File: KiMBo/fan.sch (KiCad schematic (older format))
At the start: 36 parts, among them Q4 2N7002, Q5 DMP3098L-7, Q6 2N7002, Q7 DMP3098L-7, Q8 2N7002, Q9 DMP3098L-7

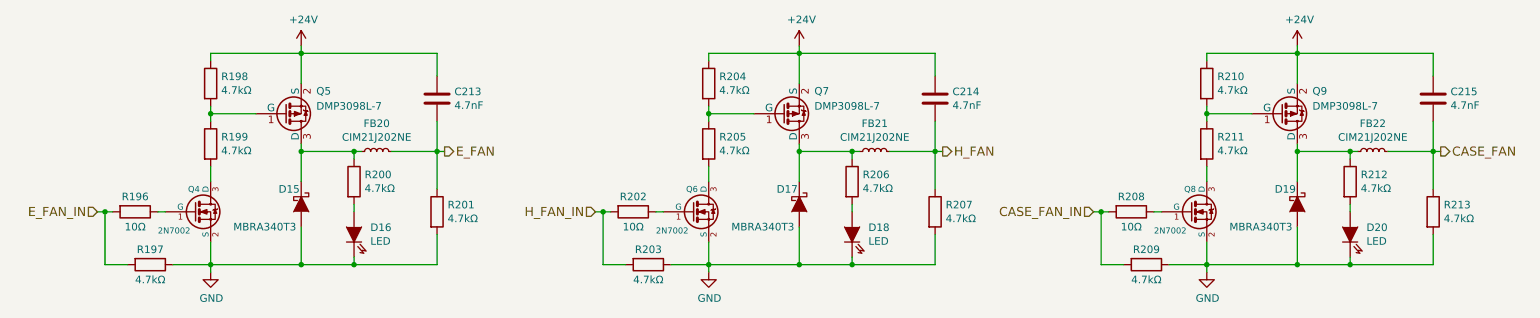
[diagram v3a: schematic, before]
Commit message: Clean up various parts of the schematic, high level sheet has annoated modules
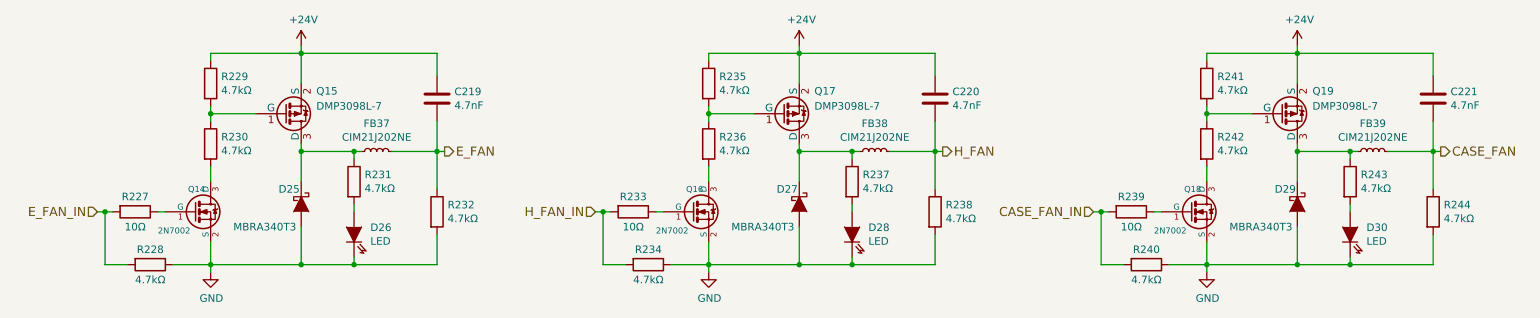
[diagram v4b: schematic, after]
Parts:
- renumbered C213 to C219, C214 to C220, C215 to C221, D15 to D25, D16 to D26, D17 to D27, D18 to D28, D19 to D29, D20 to D30, FB20 to FB37, FB21 to FB38, FB22 to FB39, Q4 to Q14, Q5 to Q15, Q6 to Q16, Q7 to Q17, Q8 to Q18, Q9 to Q19, R196 to R227, R197 to R228, R198 to R229, R199 to R230, R200 to R231, R201 to R232, R202 to R233, R203 to R234, R204 to R235, R205 to R236, R206 to R237, R207 to R238, R208 to R239, R209 to R240, R210 to R241, R211 to R242, R212 to R243, R213 to R244
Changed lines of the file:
@@
 $Descr A3 16535 11693
 encoding utf-8
-Sheet 24 26
+Sheet 26 26
 Title ""
 Date ""
@@
 $EndComp
 $Comp
-L D_Schottky D15
+L D_Schottky D25
 U 1 1 5B5EFE61
 P 4800 5550
-F 0 "D15" V 4700 5400 50  0000 L CNN
+F 0 "D25" V 4700 5400 50  0000 L CNN
 F 1 "MBRA340T3" V 4950 5100 50  0000 L CNN
 F 2 "" H 4800 5550 50  0000 C CNN
@@
 $EndComp
 $Comp
-L R R196
+L R R227
 U 1 1 5B5EFE68
 P 3700 5600
-F 0 "R196" V 3600 5600 50  0000 C CNN
+F 0 "R227" V 3600 5600 50  0000 C CNN
 F 1 "10Ω" V 3800 5600 50  0000 C CNN
 F 2 "" V 3630 5600 50  0000 C CNN
@@
 $EndComp
 $Comp
-L 2N7002P,215 Q4
+L 2N7002P,215 Q14
 U 1 1 5B5EFE6F
 P 4100 5600
-F 0 "Q4" H 4050 5750 40  0000 L CNN
+F 0 "Q14" H 4050 5750 40  0000 L CNN
 F 1 "2N7002" H 3850 5475 40  0000 L CNN
 F 2 "SOT-23" H 3970 5702 29  0001 C CNN
@@
 $EndComp
 $Comp
-L LED_Short D16
+L LED_Short D26
 U 1 1 5B5EFE77
 P 5150 5750
-F 0 "D16" V 5196 5642 50  0000 R CNN
+F 0 "D26" V 5196 5642 50  0000 R CNN
 F 1 "LED" V 5105 5642 50  0000 R CNN
 F 2 "" H 5150 5750 50  0000 C CNN
@@
 $EndComp
 $Comp
-L R R200
+L R R231
 U 1 1 5B5EFE7E
 P 5150 5400
-F 0 "R200" H 5220 5446 50  0000 L CNN
+F 0 "R231" H 5220 5446 50  0000 L CNN
 F 1 "4.7kΩ" H 5220 5355 50  0000 L CNN
 F 2 "" V 5080 5400 50  0000 C CNN
@@
 $EndComp
 $Comp
-L R R198
+L R R229
 U 1 1 5B5EFE85
 P 4200 4750
-F 0 "R198" H 4270 4796 50  0000 L CNN
+F 0 "R229" H 4270 4796 50  0000 L CNN
 F 1 "4.7kΩ" H 4270 4705 50  0000 L CNN
 F 2 "" V 4130 4750 50  0000 C CNN
@@
 $EndComp
 $Comp
-L R R199
+L R R230
 U 1 1 5B5EFE8C
 P 4200 5150
-F 0 "R199" H 4270 5196 50  0000 L CNN
+F 0 "R230" H 4270 5196 50  0000 L CNN
 F 1 "4.7kΩ" H 4270 5105 50  0000 L CNN
 F 2 "" V 4130 5150 50  0000 C CNN
@@
 $EndComp
 $Comp
-L R R197
+L R R228
 U 1 1 5B5EFE93
 P 3800 5950
-F 0 "R197" V 3700 5950 50  0000 C CNN
+F 0 "R228" V 3700 5950 50  0000 C CNN
 F 1 "4.7kΩ" V 3900 5950 50  0000 C CNN
 F 2 "" V 3730 5950 50  0000 C CNN
@@
 $EndComp
 $Comp
-L R R201
+L R R232
 U 1 1 5B5EFE9A
 P 5700 5600
-F 0 "R201" H 5770 5646 50  0000 L CNN
+F 0 "R232" H 5770 5646 50  0000 L CNN
 F 1 "4.7kΩ" H 5770 5555 50  0000 L CNN
 F 2 "" V 5630 5600 50  0000 C CNN
@@
 $EndComp
 $Comp
-L C C213
+L C C219
 U 1 1 5B5EFEA1
 P 5700 4850
-F 0 "C213" H 5815 4896 50  0000 L CNN
+F 0 "C219" H 5815 4896 50  0000 L CNN
 F 1 "4.7nF" H 5815 4805 50  0000 L CNN
 F 2 "" H 5738 4700 50  0000 C CNN
@@
 	4200 4550 5700 4550
 $Comp
-L DMP3098L-7 Q5
+L DMP3098L-7 Q15
 U 1 1 5B5EFEC7
 P 4700 4950
-F 0 "Q5" H 4900 5100 50  0000 L CNN
+F 0 "Q15" H 4900 5100 50  0000 L CNN
 F 1 "DMP3098L-7" H 4900 5000 50  0000 L CNN
 F 2 "TO_SOT_Packages_SMD:SOT-23" H 4950 5025 50  0001 L CNN
@@
 $EndComp
 $Comp
-L INDUCTOR_Small FB20
+L INDUCTOR_Small FB37
 U 1 1 5B5F15E2
 P 5300 5200
-F 0 "FB20" V 5485 5200 50  0000 C CNN
+F 0 "FB37" V 5485 5200 50  0000 C CNN
 F 1 "CIM21J202NE" V 5394 5200 50  0000 C CNN
 F 2 "" H 5300 5200 50  0000 C CNN
@@
 $EndComp
 $Comp
-L D_Schottky D17
+L D_Schottky D27
 U 1 1 5B5F23B6
 P 8100 5550
-F 0 "D17" V 8000 5400 50  0000 L CNN
+F 0 "D27" V 8000 5400 50  0000 L CNN
 F 1 "MBRA340T3" V 8250 5100 50  0000 L CNN
 F 2 "" H 8100 5550 50  0000 C CNN
@@
 $EndComp
 $Comp
-L R R202
+L R R233
 U 1 1 5B5F23BD
 P 7000 5600
-F 0 "R202" V 6900 5600 50  0000 C CNN
+F 0 "R233" V 6900 5600 50  0000 C CNN
 F 1 "10Ω" V 7100 5600 50  0000 C CNN
 F 2 "" V 6930 5600 50  0000 C CNN
@@
 $EndComp
 $Comp
-L LED_Short D18
+L LED_Short D28
 U 1 1 5B5F23CB
 P 8450 5750
-F 0 "D18" V 8496 5642 50  0000 R CNN
+F 0 "D28" V 8496 5642 50  0000 R CNN
 F 1 "LED" V 8405 5642 50  0000 R CNN
 F 2 "" H 8450 5750 50  0000 C CNN
@@
 $EndComp
 $Comp
-L R R206
+L R R237
 U 1 1 5B5F23D2
 P 8450 5400
-F 0 "R206" H 8520 5446 50  0000 L CNN
+F 0 "R237" H 8520 5446 50  0000 L CNN
 F 1 "4.7kΩ" H 8520 5355 50  0000 L CNN
 F 2 "" V 8380 5400 50  0000 C CNN
@@
 $EndComp
 $Comp
-L R R204
+L R R235
 U 1 1 5B5F23D9
 P 7500 4750
-F 0 "R204" H 7570 4796 50  0000 L CNN
+F 0 "R235" H 7570 4796 50  0000 L CNN
 F 1 "4.7kΩ" H 7570 4705 50  0000 L CNN
 F 2 "" V 7430 4750 50  0000 C CNN
@@
 $EndComp
 $Comp
-L R R205
+L R R236
 U 1 1 5B5F23E0
 P 7500 5150
-F 0 "R205" H 7570 5196 50  0000 L CNN
+F 0 "R236" H 7570 5196 50  0000 L CNN
 F 1 "4.7kΩ" H 7570 5105 50  0000 L CNN
 F 2 "" V 7430 5150 50  0000 C CNN
@@
 $EndComp
 $Comp
-L R R203
+L R R234
 U 1 1 5B5F23E7
 P 7100 5950
-F 0 "R203" V 7000 5950 50  0000 C CNN
+F 0 "R234" V 7000 5950 50  0000 C CNN
 F 1 "4.7kΩ" V 7200 5950 50  0000 C CNN
 F 2 "" V 7030 5950 50  0000 C CNN
@@
 $EndComp
 $Comp
-L R R207
+L R R238
 U 1 1 5B5F23EE
 P 9000 5600
-F 0 "R207" H 9070 5646 50  0000 L CNN
+F 0 "R238" H 9070 5646 50  0000 L CNN
 F 1 "4.7kΩ" H 9070 5555 50  0000 L CNN
 F 2 "" V 8930 5600 50  0000 C CNN
@@
 $EndComp
 $Comp
-L C C214
+L C C220
 U 1 1 5B5F23F5
 P 9000 4850
-F 0 "C214" H 9115 4896 50  0000 L CNN
+F 0 "C220" H 9115 4896 50  0000 L CNN
 F 1 "4.7nF" H 9115 4805 50  0000 L CNN
 F 2 "" H 9038 4700 50  0000 C CNN
@@
 	7500 4550 9000 4550
 $Comp
-L DMP3098L-7 Q7
+L DMP3098L-7 Q17
 U 1 1 5B5F241B
 P 8000 4950
-F 0 "Q7" H 8200 5100 50  0000 L CNN
+F 0 "Q17" H 8200 5100 50  0000 L CNN
 F 1 "DMP3098L-7" H 8200 5000 50  0000 L CNN
 F 2 "TO_SOT_Packages_SMD:SOT-23" H 8250 5025 50  0001 L CNN
@@
 $EndComp
 $Comp
-L INDUCTOR_Small FB21
+L INDUCTOR_Small FB38
 U 1 1 5B5F2422
 P 8600 5200
-F 0 "FB21" V 8785 5200 50  0000 C CNN
+F 0 "FB38" V 8785 5200 50  0000 C CNN
 F 1 "CIM21J202NE" V 8694 5200 50  0000 C CNN
 F 2 "" H 8600 5200 50  0000 C CNN
@@
 $EndComp
 $Comp
-L D_Schottky D19
+L D_Schottky D29
 U 1 1 5B5F29A1
 P 11400 5550
-F 0 "D19" V 11300 5400 50  0000 L CNN
+F 0 "D29" V 11300 5400 50  0000 L CNN
 F 1 "MBRA340T3" V 11550 5100 50  0000 L CNN
 F 2 "" H 11400 5550 50  0000 C CNN
@@
 $EndComp
 $Comp
-L R R208
+L R R239
 U 1 1 5B5F29A8
 P 10300 5600
-F 0 "R208" V 10200 5600 50  0000 C CNN
+F 0 "R239" V 10200 5600 50  0000 C CNN
 F 1 "10Ω" V 10400 5600 50  0000 C CNN
 F 2 "" V 10230 5600 50  0000 C CNN
@@
 $EndComp
 $Comp
-L LED_Short D20
+L LED_Short D30
 U 1 1 5B5F29B6
 P 11750 5750
-F 0 "D20" V 11796 5642 50  0000 R CNN
+F 0 "D30" V 11796 5642 50  0000 R CNN
 F 1 "LED" V 11705 5642 50  0000 R CNN
 F 2 "" H 11750 5750 50  0000 C CNN
@@
 $EndComp
 $Comp
-L R R212
+L R R243
 U 1 1 5B5F29BD
 P 11750 5400
-F 0 "R212" H 11820 5446 50  0000 L CNN
+F 0 "R243" H 11820 5446 50  0000 L CNN
 F 1 "4.7kΩ" H 11820 5355 50  0000 L CNN
 F 2 "" V 11680 5400 50  0000 C CNN
@@
 $EndComp
 $Comp
-L R R210
+L R R241
 U 1 1 5B5F29C4
 P 10800 4750
-F 0 "R210" H 10870 4796 50  0000 L CNN
+F 0 "R241" H 10870 4796 50  0000 L CNN
 F 1 "4.7kΩ" H 10870 4705 50  0000 L CNN
 F 2 "" V 10730 4750 50  0000 C CNN
@@
 $EndComp
 $Comp
-L R R211
+L R R242
 U 1 1 5B5F29CB
 P 10800 5150
-F 0 "R211" H 10870 5196 50  0000 L CNN
+F 0 "R242" H 10870 5196 50  0000 L CNN
 F 1 "4.7kΩ" H 10870 5105 50  0000 L CNN
 F 2 "" V 10730 5150 50  0000 C CNN
@@
 $EndComp
 $Comp
-L R R209
+L R R240
 U 1 1 5B5F29D2
 P 10400 5950
-F 0 "R209" V 10300 5950 50  0000 C CNN
+F 0 "R240" V 10300 5950 50  0000 C CNN
 F 1 "4.7kΩ" V 10500 5950 50  0000 C CNN
 F 2 "" V 10330 5950 50  0000 C CNN
@@
 $EndComp
 $Comp
-L R R213
+L R R244
 U 1 1 5B5F29D9
 P 12300 5600
-F 0 "R213" H 12370 5646 50  0000 L CNN
+F 0 "R244" H 12370 5646 50  0000 L CNN
 F 1 "4.7kΩ" H 12370 5555 50  0000 L CNN
 F 2 "" V 12230 5600 50  0000 C CNN
@@
 $EndComp
 $Comp
-L C C215
+L C C221
 U 1 1 5B5F29E0
 P 12300 4850
-F 0 "C215" H 12415 4896 50  0000 L CNN
+F 0 "C221" H 12415 4896 50  0000 L CNN
 F 1 "4.7nF" H 12415 4805 50  0000 L CNN
 F 2 "" H 12338 4700 50  0000 C CNN
@@
 	10800 4550 12300 4550
 $Comp
-L DMP3098L-7 Q9
+L DMP3098L-7 Q19
 U 1 1 5B5F2A06
 P 11300 4950
-F 0 "Q9" H 11500 5100 50  0000 L CNN
+F 0 "Q19" H 11500 5100 50  0000 L CNN
 F 1 "DMP3098L-7" H 11500 5000 50  0000 L CNN
 F 2 "TO_SOT_Packages_SMD:SOT-23" H 11550 5025 50  0001 L CNN
@@
 $EndComp
 $Comp
-L INDUCTOR_Small FB22
+L INDUCTOR_Small FB39
 U 1 1 5B5F2A0D
 P 11900 5200
-F 0 "FB22" V 12085 5200 50  0000 C CNN
+F 0 "FB39" V 12085 5200 50  0000 C CNN
 F 1 "CIM21J202NE" V 11994 5200 50  0000 C CNN
 F 2 "" H 11900 5200 50  0000 C CNN
@@
 $EndComp
 $Comp
-L 2N7002P,215 Q6
+L 2N7002P,215 Q16
 U 1 1 5B5FA7B8
 P 7400 5600
-F 0 "Q6" H 7350 5750 40  0000 L CNN
+F 0 "Q16" H 7350 5750 40  0000 L CNN
 F 1 "2N7002" H 7150 5475 40  0000 L CNN
 F 2 "SOT-23" H 7270 5702 29  0001 C CNN
@@
 $EndComp
 $Comp
-L 2N7002P,215 Q8
+L 2N7002P,215 Q18
 U 1 1 5B5FA86F
 P 10700 5600
-F 0 "Q8" H 10650 5750 40  0000 L CNN
+F 0 "Q18" H 10650 5750 40  0000 L CNN
 F 1 "2N7002" H 10450 5475 40  0000 L CNN
 F 2 "SOT-23" H 10570 5702 29  0001 C CNN

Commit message: Reorder the SS and EN lines from the shift registers such that the previously enabled/disabled motors stay enabled/disabled whilst writting to the shift register
Change 10k resistors to 4.7k, flip the open-drain inverter connected to B15 (PMTC_PGOOD)

Update the links in the README

Update the PDF schematic
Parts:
- Q14, Q16, Q18: footprint SOT-23 -> (none)
- Q15, Q17, Q19: footprint TO_SOT_Packages_SMD:SOT-23 -> (none)
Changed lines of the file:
@@
 F 0 "D25" V 4700 5400 50  0000 L CNN
 F 1 "MBRA340T3" V 4950 5100 50  0000 L CNN
-F 2 "" H 4800 5550 50  0000 C CNN
+F 2 "" H 4800 5550 50  0001 C CNN
 F 3 "" H 4800 5550 50  0000 C CNN
 	1    4800 5550
@@
 F 0 "R227" V 3600 5600 50  0000 C CNN
 F 1 "10Ω" V 3800 5600 50  0000 C CNN
-F 2 "" V 3630 5600 50  0000 C CNN
+F 2 "" V 3630 5600 50  0001 C CNN
 F 3 "" H 3700 5600 50  0000 C CNN
 	1    3700 5600
@@
 F 0 "Q14" H 4050 5750 40  0000 L CNN
 F 1 "2N7002" H 3850 5475 40  0000 L CNN
-F 2 "SOT-23" H 3970 5702 29  0001 C CNN
+F 2 "" H 3970 5702 29  0001 C CNN
 F 3 "" H 4100 5600 60  0000 C CNN
 	1    4100 5600
@@
 F 0 "D26" V 5196 5642 50  0000 R CNN
 F 1 "LED" V 5105 5642 50  0000 R CNN
-F 2 "" H 5150 5750 50  0000 C CNN
+F 2 "" H 5150 5750 50  0001 C CNN
 F 3 "" H 5150 5750 50  0000 C CNN
 	1    5150 5750
@@
 F 0 "R231" H 5220 5446 50  0000 L CNN
 F 1 "4.7kΩ" H 5220 5355 50  0000 L CNN
-F 2 "" V 5080 5400 50  0000 C CNN
+F 2 "" V 5080 5400 50  0001 C CNN
 F 3 "" H 5150 5400 50  0000 C CNN
 	1    5150 5400
@@
 F 0 "R229" H 4270 4796 50  0000 L CNN
 F 1 "4.7kΩ" H 4270 4705 50  0000 L CNN
-F 2 "" V 4130 4750 50  0000 C CNN
+F 2 "" V 4130 4750 50  0001 C CNN
 F 3 "" H 4200 4750 50  0000 C CNN
 	1    4200 4750
@@
 F 0 "R230" H 4270 5196 50  0000 L CNN
 F 1 "4.7kΩ" H 4270 5105 50  0000 L CNN
-F 2 "" V 4130 5150 50  0000 C CNN
+F 2 "" V 4130 5150 50  0001 C CNN
 F 3 "" H 4200 5150 50  0000 C CNN
 	1    4200 5150
@@
 F 0 "R228" V 3700 5950 50  0000 C CNN
 F 1 "4.7kΩ" V 3900 5950 50  0000 C CNN
-F 2 "" V 3730 5950 50  0000 C CNN
+F 2 "" V 3730 5950 50  0001 C CNN
 F 3 "" H 3800 5950 50  0000 C CNN
 	1    3800 5950
@@
 F 0 "R232" H 5770 5646 50  0000 L CNN
 F 1 "4.7kΩ" H 5770 5555 50  0000 L CNN
-F 2 "" V 5630 5600 50  0000 C CNN
+F 2 "" V 5630 5600 50  0001 C CNN
 F 3 "" H 5700 5600 50  0000 C CNN
 	1    5700 5600
@@
 F 0 "C219" H 5815 4896 50  0000 L CNN
 F 1 "4.7nF" H 5815 4805 50  0000 L CNN
-F 2 "" H 5738 4700 50  0000 C CNN
+F 2 "" H 5738 4700 50  0001 C CNN
 F 3 "" H 5700 4850 50  0000 C CNN
 	1    5700 4850
@@
 F 0 "Q15" H 4900 5100 50  0000 L CNN
 F 1 "DMP3098L-7" H 4900 5000 50  0000 L CNN
-F 2 "TO_SOT_Packages_SMD:SOT-23" H 4950 5025 50  0001 L CNN
+F 2 "" H 4950 5025 50  0001 L CNN
 F 3 "http://www.diodes.com/_files/datasheets/ds31447.pdf" H 4891 4859 50  0001 L CNN
 	1    4700 4950
@@
 F 0 "FB37" V 5485 5200 50  0000 C CNN
 F 1 "CIM21J202NE" V 5394 5200 50  0000 C CNN
-F 2 "" H 5300 5200 50  0000 C CNN
+F 2 "" H 5300 5200 50  0001 C CNN
 F 3 "" H 5300 5200 50  0000 C CNN
 	1    5300 5200
@@
 F 0 "D27" V 8000 5400 50  0000 L CNN
 F 1 "MBRA340T3" V 8250 5100 50  0000 L CNN
-F 2 "" H 8100 5550 50  0000 C CNN
+F 2 "" H 8100 5550 50  0001 C CNN
 F 3 "" H 8100 5550 50  0000 C CNN
 	1    8100 5550
@@
 F 0 "R233" V 6900 5600 50  0000 C CNN
 F 1 "10Ω" V 7100 5600 50  0000 C CNN
-F 2 "" V 6930 5600 50  0000 C CNN
+F 2 "" V 6930 5600 50  0001 C CNN
 F 3 "" H 7000 5600 50  0000 C CNN
 	1    7000 5600
@@
 F 0 "D28" V 8496 5642 50  0000 R CNN
 F 1 "LED" V 8405 5642 50  0000 R CNN
-F 2 "" H 8450 5750 50  0000 C CNN
+F 2 "" H 8450 5750 50  0001 C CNN
 F 3 "" H 8450 5750 50  0000 C CNN
 	1    8450 5750
@@
 F 0 "R237" H 8520 5446 50  0000 L CNN
 F 1 "4.7kΩ" H 8520 5355 50  0000 L CNN
-F 2 "" V 8380 5400 50  0000 C CNN
+F 2 "" V 8380 5400 50  0001 C CNN
 F 3 "" H 8450 5400 50  0000 C CNN
 	1    8450 5400
@@
 F 0 "R235" H 7570 4796 50  0000 L CNN
 F 1 "4.7kΩ" H 7570 4705 50  0000 L CNN
-F 2 "" V 7430 4750 50  0000 C CNN
+F 2 "" V 7430 4750 50  0001 C CNN
 F 3 "" H 7500 4750 50  0000 C CNN
 	1    7500 4750
@@
 F 0 "R236" H 7570 5196 50  0000 L CNN
 F 1 "4.7kΩ" H 7570 5105 50  0000 L CNN
-F 2 "" V 7430 5150 50  0000 C CNN
+F 2 "" V 7430 5150 50  0001 C CNN
 F 3 "" H 7500 5150 50  0000 C CNN
 	1    7500 5150
@@
 F 0 "R234" V 7000 5950 50  0000 C CNN
 F 1 "4.7kΩ" V 7200 5950 50  0000 C CNN
-F 2 "" V 7030 5950 50  0000 C CNN
+F 2 "" V 7030 5950 50  0001 C CNN
 F 3 "" H 7100 5950 50  0000 C CNN
 	1    7100 5950
@@
 F 0 "R238" H 9070 5646 50  0000 L CNN
 F 1 "4.7kΩ" H 9070 5555 50  0000 L CNN
-F 2 "" V 8930 5600 50  0000 C CNN
+F 2 "" V 8930 5600 50  0001 C CNN
 F 3 "" H 9000 5600 50  0000 C CNN
 	1    9000 5600
@@
 F 0 "C220" H 9115 4896 50  0000 L CNN
 F 1 "4.7nF" H 9115 4805 50  0000 L CNN
-F 2 "" H 9038 4700 50  0000 C CNN
+F 2 "" H 9038 4700 50  0001 C CNN
 F 3 "" H 9000 4850 50  0000 C CNN
 	1    9000 4850
@@
 F 0 "Q17" H 8200 5100 50  0000 L CNN
 F 1 "DMP3098L-7" H 8200 5000 50  0000 L CNN
-F 2 "TO_SOT_Packages_SMD:SOT-23" H 8250 5025 50  0001 L CNN
+F 2 "" H 8250 5025 50  0001 L CNN
 F 3 "http://www.diodes.com/_files/datasheets/ds31447.pdf" H 8191 4859 50  0001 L CNN
 	1    8000 4950
@@
 F 0 "FB38" V 8785 5200 50  0000 C CNN
 F 1 "CIM21J202NE" V 8694 5200 50  0000 C CNN
-F 2 "" H 8600 5200 50  0000 C CNN
+F 2 "" H 8600 5200 50  0001 C CNN
 F 3 "" H 8600 5200 50  0000 C CNN
 	1    8600 5200
@@
 F 0 "D29" V 11300 5400 50  0000 L CNN
 F 1 "MBRA340T3" V 11550 5100 50  0000 L CNN
-F 2 "" H 11400 5550 50  0000 C CNN
+F 2 "" H 11400 5550 50  0001 C CNN
 F 3 "" H 11400 5550 50  0000 C CNN
 	1    11400 5550
@@
 F 0 "R239" V 10200 5600 50  0000 C CNN
 F 1 "10Ω" V 10400 5600 50  0000 C CNN
-F 2 "" V 10230 5600 50  0000 C CNN
+F 2 "" V 10230 5600 50  0001 C CNN
 F 3 "" H 10300 5600 50  0000 C CNN
 	1    10300 5600
@@
 F 0 "D30" V 11796 5642 50  0000 R CNN
 F 1 "LED" V 11705 5642 50  0000 R CNN
-F 2 "" H 11750 5750 50  0000 C CNN
+F 2 "" H 11750 5750 50  0001 C CNN
 F 3 "" H 11750 5750 50  0000 C CNN
 	1    11750 5750
@@
 F 0 "R243" H 11820 5446 50  0000 L CNN
 F 1 "4.7kΩ" H 11820 5355 50  0000 L CNN
-F 2 "" V 11680 5400 50  0000 C CNN
+F 2 "" V 11680 5400 50  0001 C CNN
 F 3 "" H 11750 5400 50  0000 C CNN
 	1    11750 5400
@@
 F 0 "R241" H 10870 4796 50  0000 L CNN
 F 1 "4.7kΩ" H 10870 4705 50  0000 L CNN
-F 2 "" V 10730 4750 50  0000 C CNN
+F 2 "" V 10730 4750 50  0001 C CNN
 F 3 "" H 10800 4750 50  0000 C CNN
 	1    10800 4750
@@
 F 0 "R242" H 10870 5196 50  0000 L CNN
 F 1 "4.7kΩ" H 10870 5105 50  0000 L CNN
-F 2 "" V 10730 5150 50  0000 C CNN
+F 2 "" V 10730 5150 50  0001 C CNN
 F 3 "" H 10800 5150 50  0000 C CNN
 	1    10800 5150
@@
 F 0 "R240" V 10300 5950 50  0000 C CNN
 F 1 "4.7kΩ" V 10500 5950 50  0000 C CNN
-F 2 "" V 10330 5950 50  0000 C CNN
+F 2 "" V 10330 5950 50  0001 C CNN
 F 3 "" H 10400 5950 50  0000 C CNN
 	1    10400 5950
@@
 F 0 "R244" H 12370 5646 50  0000 L CNN
 F 1 "4.7kΩ" H 12370 5555 50  0000 L CNN
-F 2 "" V 12230 5600 50  0000 C CNN
+F 2 "" V 12230 5600 50  0001 C CNN
 F 3 "" H 12300 5600 50  0000 C CNN
 	1    12300 5600
@@
 F 0 "C221" H 12415 4896 50  0000 L CNN
 F 1 "4.7nF" H 12415 4805 50  0000 L CNN
-F 2 "" H 12338 4700 50  0000 C CNN
+F 2 "" H 12338 4700 50  0001 C CNN
 F 3 "" H 12300 4850 50  0000 C CNN
 	1    12300 4850
@@
 F 0 "Q19" H 11500 5100 50  0000 L CNN
 F 1 "DMP3098L-7" H 11500 5000 50  0000 L CNN
-F 2 "TO_SOT_Packages_SMD:SOT-23" H 11550 5025 50  0001 L CNN
+F 2 "" H 11550 5025 50  0001 L CNN
 F 3 "http://www.diodes.com/_files/datasheets/ds31447.pdf" H 11491 4859 50  0001 L CNN
 	1    11300 4950
@@
 F 0 "FB39" V 12085 5200 50  0000 C CNN
 F 1 "CIM21J202NE" V 11994 5200 50  0000 C CNN
-F 2 "" H 11900 5200 50  0000 C CNN
+F 2 "" H 11900 5200 50  0001 C CNN
 F 3 "" H 11900 5200 50  0000 C CNN
 	1    11900 5200
@@
 F 0 "Q16" H 7350 5750 40  0000 L CNN
 F 1 "2N7002" H 7150 5475 40  0000 L CNN
-F 2 "SOT-23" H 7270 5702 29  0001 C CNN
+F 2 "" H 7270 5702 29  0001 C CNN
 F 3 "" H 7400 5600 60  0000 C CNN
 	1    7400 5600
@@
 F 0 "Q18" H 10650 5750 40  0000 L CNN
 F 1 "2N7002" H 10450 5475 40  0000 L CNN
-F 2 "SOT-23" H 10570 5702 29  0001 C CNN
+F 2 "" H 10570 5702 29  0001 C CNN
 F 3 "" H 10700 5600 60  0000 C CNN
 	1    10700 5600
